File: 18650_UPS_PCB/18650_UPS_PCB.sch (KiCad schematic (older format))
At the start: 43 parts, among them J1 USB_B_Micro, J2 Conn_01x02, J3 Conn_01x02, SW1 SW_DIP_x02, U1 STLINK-V3MINI, U10 LR9102G-xx, U11 MP2667, U2 INA237, U3 EA_DOGS104N-A, U5 STM32L151RCTx

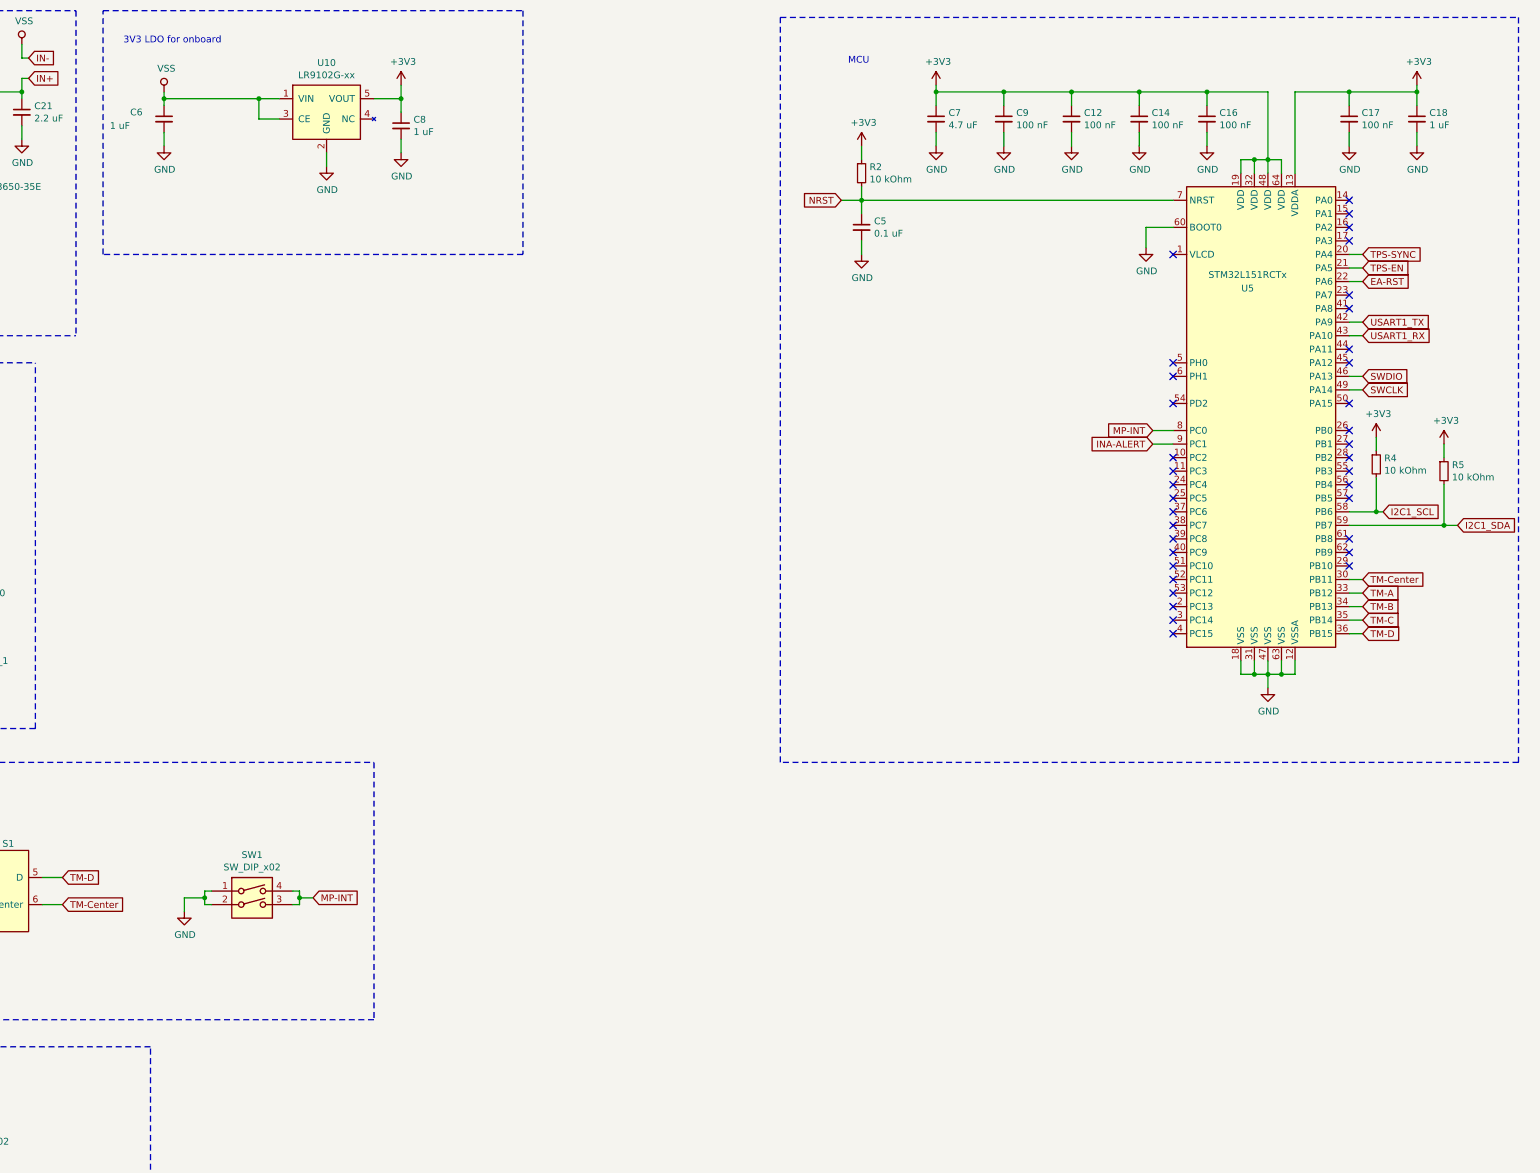
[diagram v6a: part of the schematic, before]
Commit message: minor changes in layout
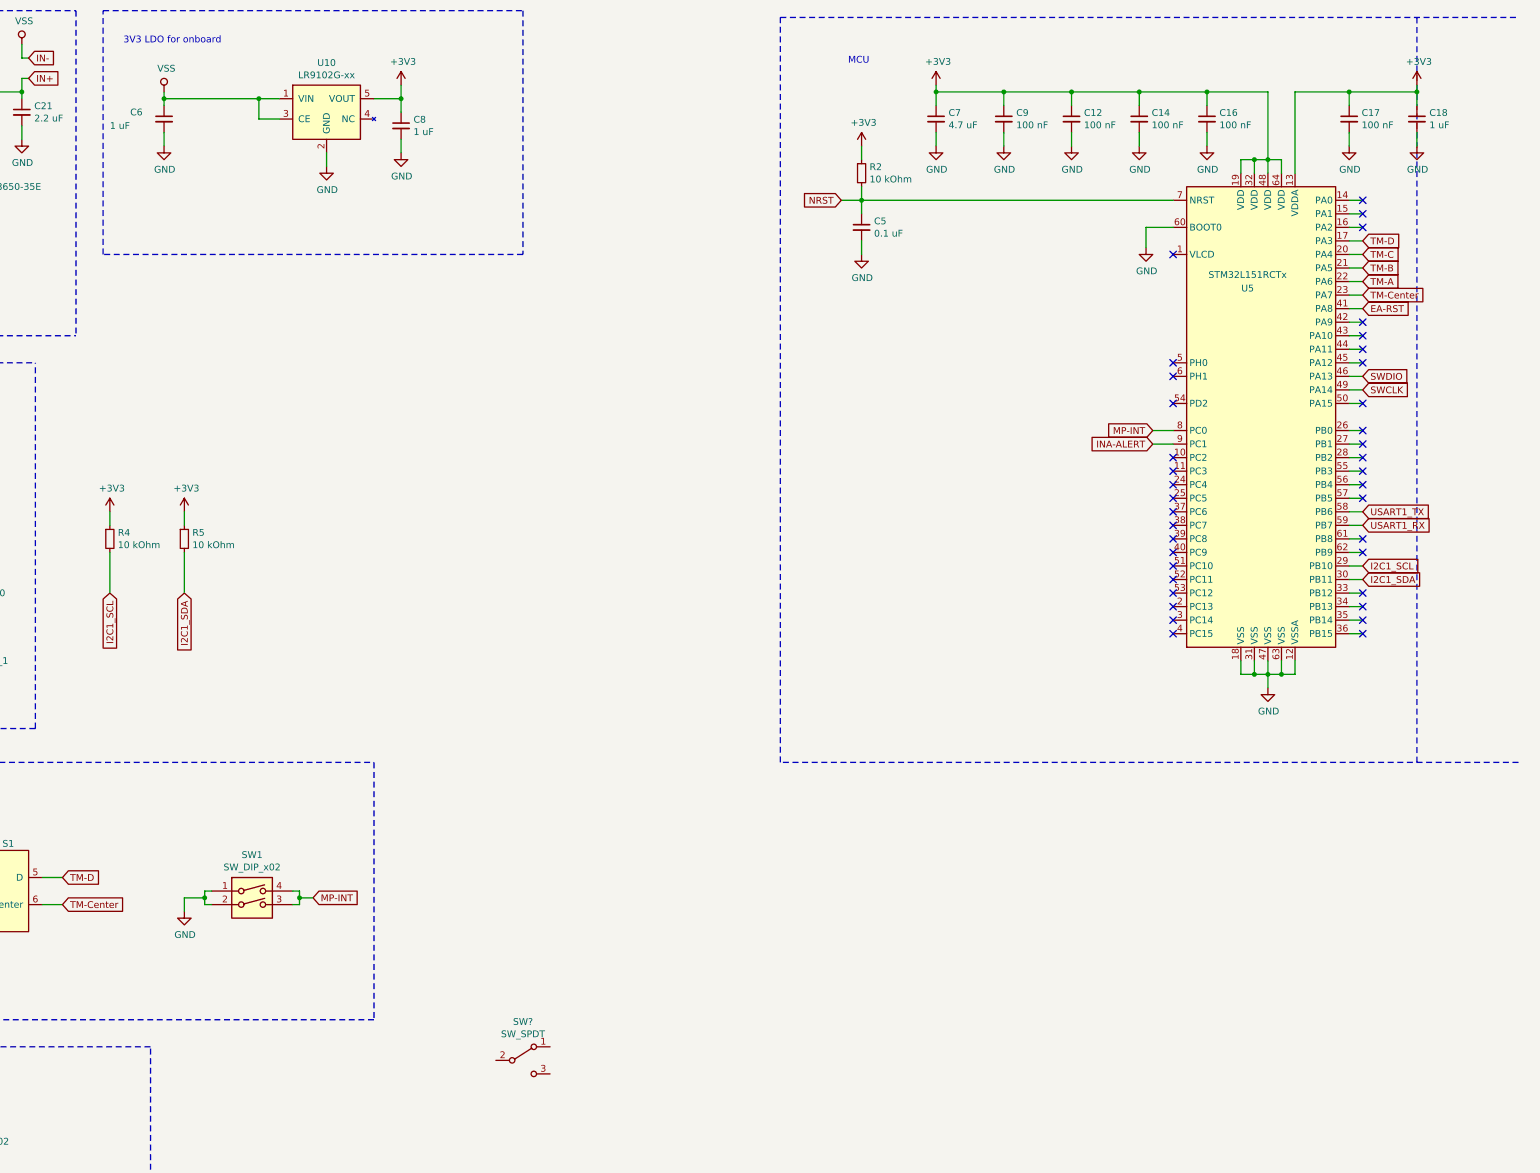
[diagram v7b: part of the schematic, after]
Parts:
- added SW?: SW_SPDT, symbol Switch:SW_SPDT
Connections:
- net TPS-EN is gone; now on net TM-B: U5.21 (PA5)
- net TPS-SYNC is gone; now on net TM-C: U5.20 (PA4)
- net EA-RST: now also U5.41 (PA8); no longer U5.22 (PA6)
- net I2C1_SCL: now also U5.29 (PB10); no longer U5.58 (PB6)
- net I2C1_SDA: now also U5.30 (PB11); no longer U5.59 (PB7)
- net TM-A: now also U5.22 (PA6); no longer U5.33 (PB12)
- net TM-B: no longer U5.34 (PB13)
- net TM-C: no longer U5.35 (PB14)
- net TM-Center: now also U5.23 (PA7); no longer U5.30 (PB11)
- net TM-D: now also U5.17 (PA3); no longer U5.36 (PB15)
- net USART1_RX: now also U5.59 (PB7); no longer U5.43 (PA10)
- net USART1_TX: now also U5.58 (PB6); no longer U5.42 (PA9)
- no-connect marks 45 -> 47
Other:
- moved on the sheet: R4, R5
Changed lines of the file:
@@
 Text GLabel 13150 3750 0    50   Input ~ 0
 MP-INT
-Text GLabel 14850 4350 2    50   Input ~ 0
-I2C1_SCL
-Text GLabel 15400 4450 2    50   Input ~ 0
-I2C1_SDA
-Text GLabel 14700 3050 2    50   Input ~ 0
+Text GLabel 14700 4450 2    50   Input ~ 0
 USART1_RX
 Text GLabel 14700 3450 2    50   Input ~ 0
@@
 Text GLabel 14700 3350 2    50   Input ~ 0
 SWDIO
-Text GLabel 14700 2950 2    50   Input ~ 0
+Text GLabel 14700 4350 2    50   Input ~ 0
 USART1_TX
 Text GLabel 10850 2050 0    50   Input ~ 0
 NRST
-Text GLabel 14700 2650 2    50   Input ~ 0
+Text GLabel 14700 2850 2    50   Input ~ 0
 EA-RST
 $Comp
@@
 Wire Wire Line
 	3850 7250 4050 7250
-Text GLabel 14700 4950 2    50   Input ~ 0
+Text GLabel 14700 2650 2    50   Input ~ 0
 TM-A
-Text GLabel 14700 5050 2    50   Input ~ 0
+Text GLabel 14700 2550 2    50   Input ~ 0
 TM-B
-Text GLabel 14700 5150 2    50   Input ~ 0
+Text GLabel 14700 2450 2    50   Input ~ 0
 TM-C
-Text GLabel 14700 5250 2    50   Input ~ 0
+Text GLabel 14700 2350 2    50   Input ~ 0
 TM-D
-Text GLabel 14700 4850 2    50   Input ~ 0
+Text GLabel 14700 2750 2    50   Input ~ 0
 TM-Center
 Text Notes 3800 6450 0    50   ~ 0
@@
 Wire Wire Line
 	3950 8900 3950 8850
-Text GLabel 14700 2450 2    50   Input ~ 0
-TPS-SYNC
-Text GLabel 14700 2550 2    50   Input ~ 0
-TPS-EN
 $Comp
 L Device:C_Small C?
@@
 	14700 3450 14600 3450
 Wire Wire Line
-	14700 2950 14600 2950
-Wire Wire Line
-	14700 3050 14600 3050
-Wire Wire Line
-	14700 4850 14600 4850
-Wire Wire Line
-	14600 4950 14700 4950
-Wire Wire Line
-	14700 5050 14600 5050
-Wire Wire Line
-	14600 5150 14700 5150
-Wire Wire Line
-	14700 5250 14600 5250
+	14700 4350 14600 4350
+Wire Wire Line
+	14700 4450 14600 4450
+Wire Wire Line
+	14700 2750 14600 2750
+Wire Wire Line
+	14600 2650 14700 2650
+Wire Wire Line
+	14700 2550 14600 2550
+Wire Wire Line
+	14600 2450 14700 2450
+Wire Wire Line
+	14700 2350 14600 2350
 Wire Wire Line
 	13150 3750 13300 3750
@@
 	13300 3850 13150 3850
 Wire Wire Line
-	14700 2450 14600 2450
-Wire Wire Line
-	14600 2550 14700 2550
-Wire Wire Line
-	14700 2650 14600 2650
-NoConn ~ 14600 2050
-NoConn ~ 14600 2150
-NoConn ~ 14600 2250
-NoConn ~ 14600 2350
-NoConn ~ 14600 2750
-NoConn ~ 14600 2850
-NoConn ~ 14600 3150
-NoConn ~ 14600 3250
-NoConn ~ 14600 3550
-NoConn ~ 14600 3750
-NoConn ~ 14600 3850
-NoConn ~ 14600 3950
-NoConn ~ 14600 4050
-NoConn ~ 14600 4150
-NoConn ~ 14600 4250
-NoConn ~ 14600 4750
-NoConn ~ 14600 4650
-NoConn ~ 14600 4550
+	14700 2850 14600 2850
 NoConn ~ 13300 5250
 NoConn ~ 13300 5150
@@
 	10400 700  15850 700
 Wire Notes Line
-	15850 700  15850 6200
-Wire Notes Line
 	15850 6200 10400 6200
 Wire Notes Line
@@
 Wire Wire Line
 	2850 4600 2850 4500
+Wire Wire Line
+	5450 4450 5450 4350
+$Comp
+L power:+3V3 #PWR0136
+U 1 1 613C9614
+P 5450 4350
+F 0 "#PWR0136" H 5450 4200 50  0001 C CNN
+F 1 "+3V3" H 5465 4523 50  0000 C CNN
+F 2 "" H 5450 4350 50  0001 C CNN
+F 3 "" H 5450 4350 50  0001 C CNN
+	1    5450 4350
+	1    0    0    -1
+$EndComp
+$Comp
+L Device:R_Small R?
+U 1 1 613C960D
+P 5450 4550
+AR Path="/609F1585/613C960D" Ref="R?"  Part="1"
+AR Path="/613C960D" Ref="R4"  Part="1"
+F 0 "R4" H 5509 4596 50  0000 L CNN
+F 1 "10 kOhm" H 5509 4505 50  0000 L CNN
+F 2 "Resistor_SMD:R_0603_1608Metric" H 5450 4550 50  0001 C CNN
+F 3 "~" H 5450 4550 50  0001 C CNN
+	1    5450 4550
+	1    0    0    -1
+$EndComp
+Wire Wire Line
+	6000 4650 6000 4950
+Wire Wire Line
+	6000 4450 6000 4350
+$Comp
+L power:+3V3 #PWR0135
+U 1 1 6138CC09
+P 6000 4350
+F 0 "#PWR0135" H 6000 4200 50  0001 C CNN
+F 1 "+3V3" H 6015 4523 50  0000 C CNN
+F 2 "" H 6000 4350 50  0001 C CNN
+F 3 "" H 6000 4350 50  0001 C CNN
+	1    6000 4350
+	1    0    0    -1
+$EndComp
 $Comp
 L Device:R_Small R?
 U 1 1 6138CC02
-P 15300 4050
+P 6000 4550
 AR Path="/609F1585/6138CC02" Ref="R?"  Part="1"
 AR Path="/6138CC02" Ref="R5"  Part="1"
-F 0 "R5" H 15359 4096 50  0000 L CNN
-F 1 "10 kOhm" H 15359 4005 50  0000 L CNN
-F 2 "Resistor_SMD:R_0603_1608Metric" H 15300 4050 50  0001 C CNN
-F 3 "~" H 15300 4050 50  0001 C CNN
-	1    15300 4050
-	1    0    0    -1
-$EndComp
-$Comp
-L power:+3V3 #PWR0135
-U 1 1 6138CC09
-P 15300 3850
-F 0 "#PWR0135" H 15300 3700 50  0001 C CNN
-F 1 "+3V3" H 15315 4023 50  0000 C CNN
-F 2 "" H 15300 3850 50  0001 C CNN
-F 3 "" H 15300 3850 50  0001 C CNN
-	1    15300 3850
-	1    0    0    -1
-$EndComp
-Wire Wire Line
-	15300 3950 15300 3850
-Wire Wire Line
-	15300 4150 15300 4450
-Connection ~ 15300 4450
-Wire Wire Line
-	15300 4450 15400 4450
-$Comp
-L Device:R_Small R?
-U 1 1 613C960D
-P 14800 4000
-AR Path="/609F1585/613C960D" Ref="R?"  Part="1"
-AR Path="/613C960D" Ref="R4"  Part="1"
-F 0 "R4" H 14859 4046 50  0000 L CNN
-F 1 "10 kOhm" H 14859 3955 50  0000 L CNN
-F 2 "Resistor_SMD:R_0603_1608Metric" H 14800 4000 50  0001 C CNN
-F 3 "~" H 14800 4000 50  0001 C CNN
-	1    14800 4000
-	1    0    0    -1
-$EndComp
-$Comp
-L power:+3V3 #PWR0136
-U 1 1 613C9614
-P 14800 3800
-F 0 "#PWR0136" H 14800 3650 50  0001 C CNN
-F 1 "+3V3" H 14815 3973 50  0000 C CNN
-F 2 "" H 14800 3800 50  0001 C CNN
-F 3 "" H 14800 3800 50  0001 C CNN
-	1    14800 3800
-	1    0    0    -1
-$EndComp
-Wire Wire Line
-	14800 3900 14800 3800
-Wire Wire Line
-	14600 4450 15300 4450
-Wire Wire Line
-	14600 4350 14800 4350
-Wire Wire Line
-	14800 4100 14800 4350
-Connection ~ 14800 4350
-Wire Wire Line
-	14800 4350 14850 4350
+F 0 "R5" H 6059 4596 50  0000 L CNN
+F 1 "10 kOhm" H 6059 4505 50  0000 L CNN
+F 2 "Resistor_SMD:R_0603_1608Metric" H 6000 4550 50  0001 C CNN
+F 3 "~" H 6000 4550 50  0001 C CNN
+	1    6000 4550
+	1    0    0    -1
+$EndComp
+Wire Notes Line
+	15100 700  15100 6200
+Text GLabel 14700 4850 2    50   Input ~ 0
+I2C1_SDA
+Text GLabel 14700 4750 2    50   Input ~ 0
+I2C1_SCL
+Text GLabel 5450 4950 3    50   Input ~ 0
+I2C1_SCL
+Text GLabel 6000 4950 3    50   Input ~ 0
+I2C1_SDA
+Wire Wire Line
+	5450 4650 5450 4950
+Wire Wire Line
+	14700 4750 14600 4750
+Wire Wire Line
+	14600 4850 14700 4850
+NoConn ~ 14700 2950
+NoConn ~ 14700 3050
+NoConn ~ 14700 3150
+NoConn ~ 14700 3250
+NoConn ~ 14700 3550
+NoConn ~ 14700 3750
+NoConn ~ 14700 3850
+NoConn ~ 14700 3950
+NoConn ~ 14700 4050
+NoConn ~ 14700 4150
+NoConn ~ 14700 4250
+NoConn ~ 14700 4550
+NoConn ~ 14700 4650
+NoConn ~ 14700 4950
+NoConn ~ 14700 5050
+NoConn ~ 14700 5150
+NoConn ~ 14700 5250
+Wire Wire Line
+	14600 5250 14700 5250
+Wire Wire Line
+	14600 5150 14700 5150
+Wire Wire Line
+	14600 5050 14700 5050
+Wire Wire Line
+	14700 4950 14600 4950
+Wire Wire Line
+	14700 4650 14600 4650
+Wire Wire Line
+	14700 4550 14600 4550
+Wire Wire Line
+	14700 4250 14600 4250
+Wire Wire Line
+	14600 4150 14700 4150
+Wire Wire Line
+	14700 4050 14600 4050
+Wire Wire Line
+	14600 3950 14700 3950
+Wire Wire Line
+	14700 3850 14600 3850
+Wire Wire Line
+	14600 3750 14700 3750
+Wire Wire Line
+	14700 3550 14600 3550
+Wire Wire Line
+	14600 3250 14700 3250
+Wire Wire Line
+	14700 3150 14600 3150
+Wire Wire Line
+	14600 3050 14700 3050
+Wire Wire Line
+	14600 2950 14700 2950
+Wire Wire Line
+	14600 2250 14700 2250
+Wire Wire Line
+	14600 2150 14700 2150
+Wire Wire Line
+	14600 2050 14700 2050
+NoConn ~ 14700 2050
+NoConn ~ 14700 2150
+NoConn ~ 14700 2250
+$Comp
+L Switch:SW_SPDT SW?
+U 1 1 614E8F27
+P 8500 8400
+F 0 "SW?" H 8500 8685 50  0000 C CNN
+F 1 "SW_SPDT" H 8500 8594 50  0000 C CNN
+F 2 "" H 8500 8400 50  0001 C CNN
+F 3 "~" H 8500 8400 50  0001 C CNN
+	1    8500 8400
+	1    0    0    -1
+$EndComp
 $EndSCHEMATC
